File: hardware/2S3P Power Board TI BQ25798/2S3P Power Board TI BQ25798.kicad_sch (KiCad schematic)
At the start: 1 part, among them U1 BQ25798RQMR

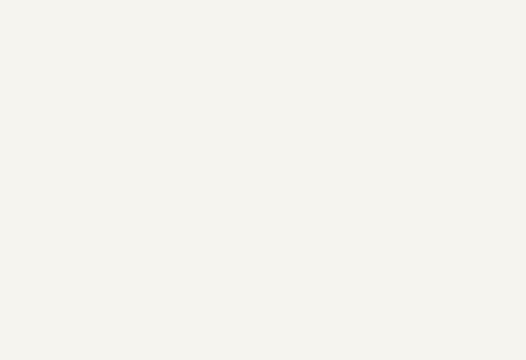
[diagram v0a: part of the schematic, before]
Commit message: Selected USB PD chip
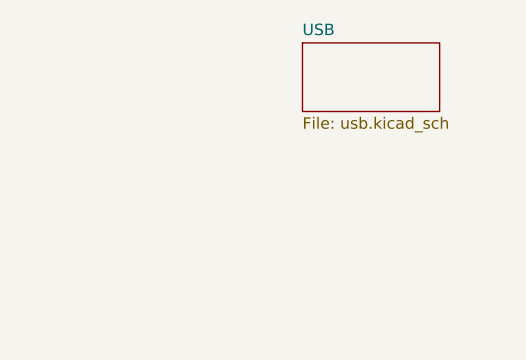
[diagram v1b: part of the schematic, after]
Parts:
- U1: MPN (none) -> C2876593
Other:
- added sheet USB (usb.kicad_sch)
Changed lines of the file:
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@@
       (effects (font (size 1.27 1.27) italic) hide)
+    )
+    (property "MPN" "C2876593" (at 119.38 58.42 0)
+      (effects (font (size 1.27 1.27)) hide)
     )
     (pin "2")
@@
       )
     )
+  )
+  (sheet (at 245.11 16.51) (size 15.24 7.62) (fields_autoplaced)
+    (stroke (width 0.1524) (type solid))
+    (fill (color 0 0 0 0.0000))
+    (property "Sheetname" "USB" (at 245.11 15.7984 0)
+      (effects (font (size 1.27 1.27)) (justify left bottom))
+    )
+    (property "Sheetfile" "usb.kicad_sch" (at 245.11 24.7146 0)
+      (effects (font (size 1.27 1.27)) (justify left top))
+    )
+    (instances
+      (project "2S3P Power Board TI BQ25798"
+        (path "/d7fbba2e-84c5-4e09-9d36-52dae726d12d" (page "2"))
+      )
+    )

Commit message: Checkpointing progress
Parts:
- renumbered U1 to U201
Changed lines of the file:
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@@
   (symbol (lib_id "TI BQ25798:BQ25798RQMR") (at 119.38 58.42 0) (unit 1)
     (in_bom yes) (on_board yes) (dnp no) (fields_autoplaced)
-    (property "Reference" "U1" (at 142.24 48.26 0)
+    (property "Reference" "U201" (at 142.24 48.26 0)
       (effects (font (size 1.524 1.524)))
     )
@@
       (project "2S3P Power Board TI BQ25798"
         (path "/d7fbba2e-84c5-4e09-9d36-52dae726d12d"
-          (reference "U1") (unit 1)
+          (reference "U201") (unit 1)
         )
       )

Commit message: First draft of USB section
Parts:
- U201: Manufacturer (none) -> TEXAS INSTRUMENTS; Manufacturer Part Number (none) -> BQ25798RQMR
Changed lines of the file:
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@@
+      (effects (font (size 1.27 1.27)) hide)
+    )
+    (property "Manufacturer" "TEXAS INSTRUMENTS" (at 119.38 58.42 0)
+      (effects (font (size 1.27 1.27)) hide)
+    )
+    (property "Manufacturer Part Number" "BQ25798RQMR" (at 119.38 58.42 0)
       (effects (font (size 1.27 1.27)) hide)
     )

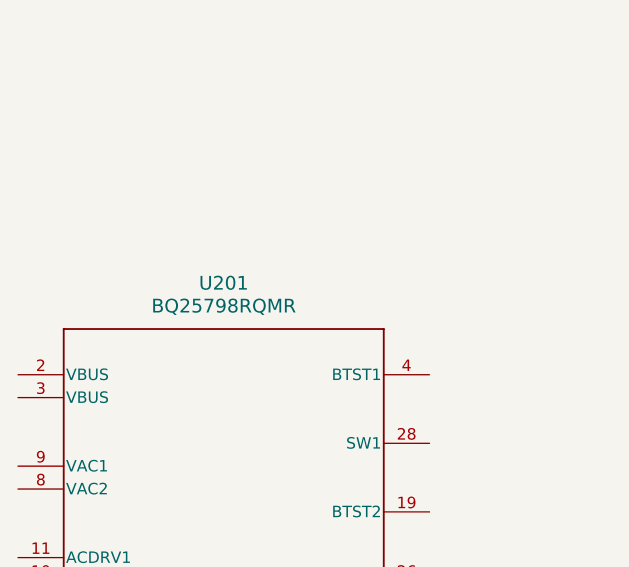
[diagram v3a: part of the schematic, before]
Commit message: Fix part numbering
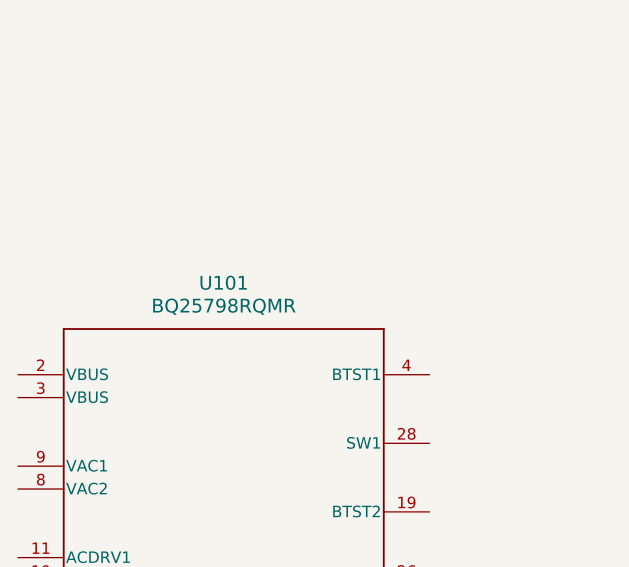
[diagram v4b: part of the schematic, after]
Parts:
- renumbered U201 to U101
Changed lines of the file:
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@@
   (symbol (lib_id "TI BQ25798:BQ25798RQMR") (at 119.38 58.42 0) (unit 1)
     (in_bom yes) (on_board yes) (dnp no) (fields_autoplaced)
-    (property "Reference" "U201" (at 142.24 48.26 0)
+    (property "Reference" "U101" (at 142.24 48.26 0)
       (effects (font (size 1.524 1.524)))
     )
@@
       (project "2S3P Power Board TI BQ25798"
         (path "/d7fbba2e-84c5-4e09-9d36-52dae726d12d"
-          (reference "U201") (unit 1)
+          (reference "U101") (unit 1)
         )
       )

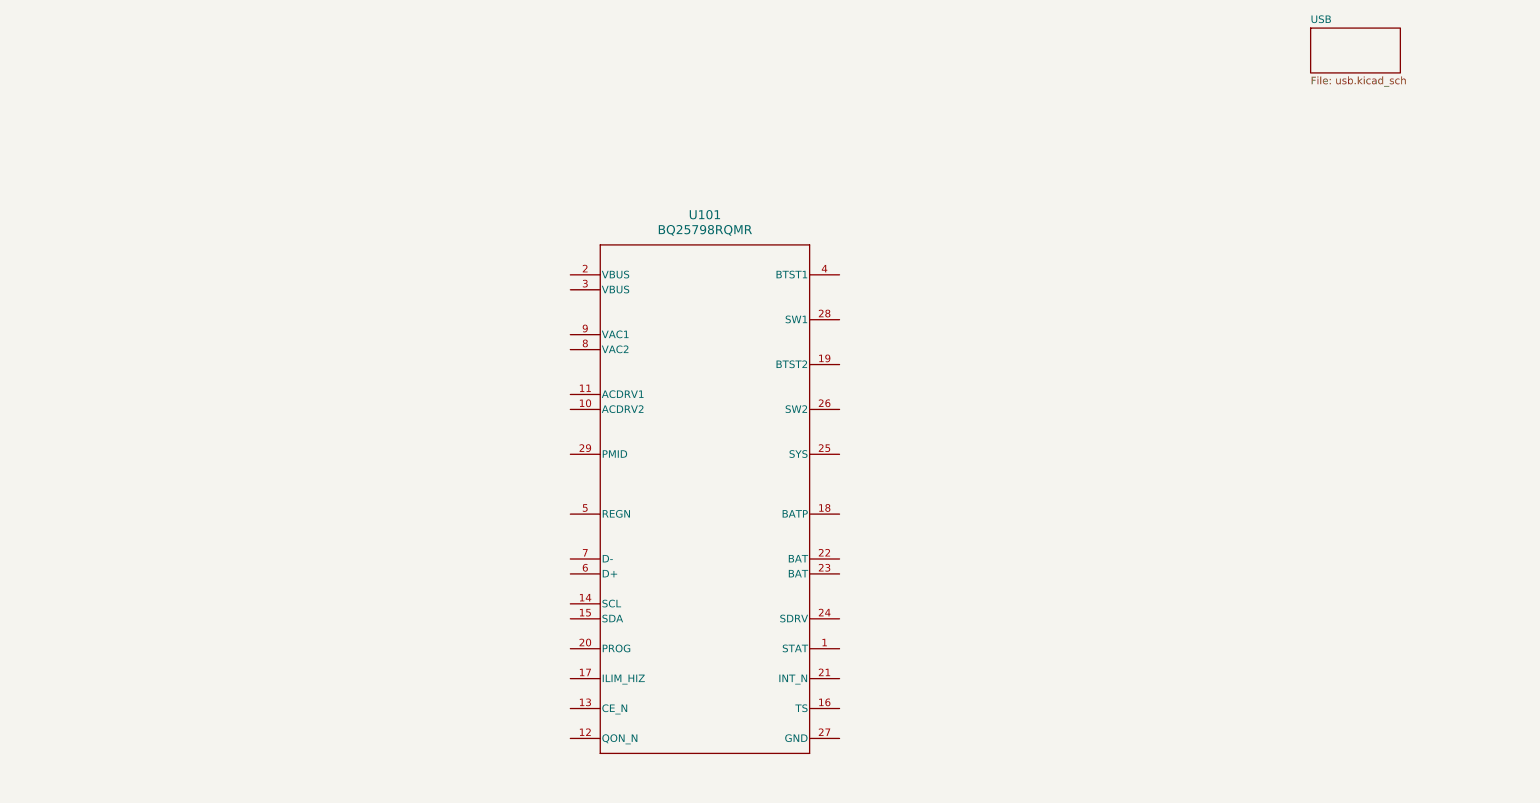
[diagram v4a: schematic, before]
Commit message: Set up input selection into the BQ25798
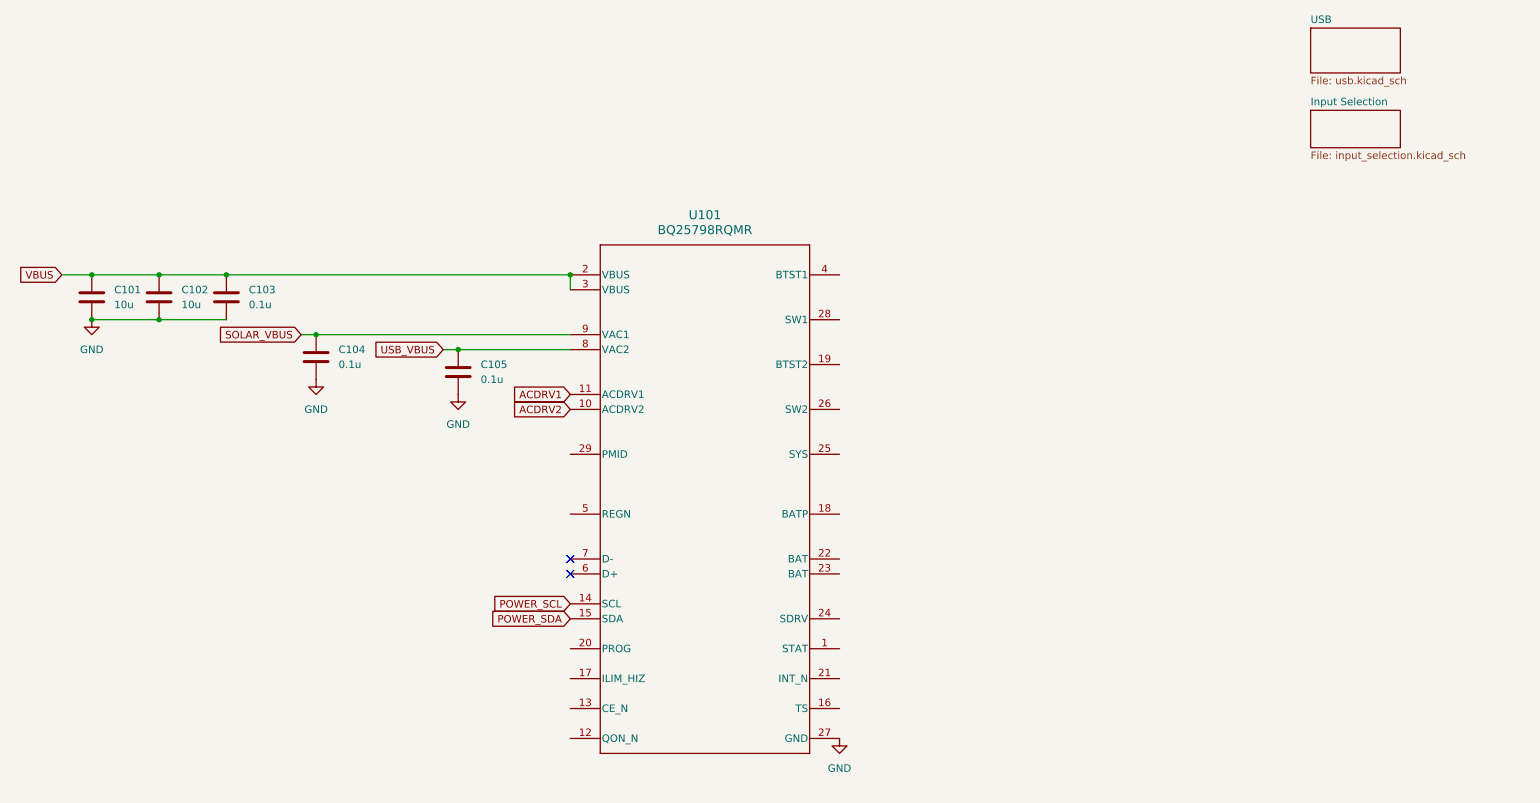
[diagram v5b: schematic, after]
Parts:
- added C101, C102: 10u, Capacitor_SMD:C_0805_2012Metric, symbol Device:C
- added C103, C104, C105: 0.1u, Capacitor_SMD:C_0402_1005Metric, symbol Device:C
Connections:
- net ACDRV2: now reaches U101.10 (ACDRV2)
- net ACDRV1: now reaches U101.11 (ACDRV1)
- net POWER_SCL: now reaches U101.14 (SCL)
- net POWER_SDA: now reaches U101.15 (SDA)
- net VBUS: now reaches U101.2 (VBUS)
- net VBUS: now also U101.3 (VBUS), C101.1, C102.1, C103.1
- net GND: now reaches U101.27 (GND)
- net GND: now also C101.2, C102.2, C103.2, C104.2, C105.2
- net USB_VBUS: now reaches U101.8 (VAC2)
- net USB_VBUS: now also C105.1
- net SOLAR_VBUS: now reaches U101.9 (VAC1)
- net SOLAR_VBUS: now also C104.1
- no-connect marks 0 -> 2
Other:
- added sheet Input Selection (input_selection.kicad_sch)

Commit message: Filled in part numbers
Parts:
- C101, C102: Designed Manufacturer (none) -> TDK; Designed Part Number (none) -> C2012X5R1E106K125AB; MPN (none) -> C386087; Manufacturer TDK -> Taiyo Yuden; Manufacturer Part Number C2012X5R1E106K125AB -> TMK212BJ106KG-TD
- C103, C104, C105: Designed Manufacturer (none) -> TDK; Designed Part Number (none) -> C1005X7R1H104K050BE; MPN (none) -> C5142579; Manufacturer TDK -> CCTC; Manufacturer Part Number C1005X7R1H104K050BE -> TCC0402X5R104K500AT
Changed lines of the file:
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@@
       (effects (font (size 1.27 1.27)) hide)
     )
-    (property "Manufacturer" "TDK" (at 49.53 62.23 0)
-      (effects (font (size 1.27 1.27)) hide)
-    )
-    (property "Manufacturer Part Number" "C2012X5R1E106K125AB " (at 49.53 62.23 0)
+    (property "Manufacturer" "Taiyo Yuden" (at 49.53 62.23 0)
+      (effects (font (size 1.27 1.27)) hide)
+    )
+    (property "Manufacturer Part Number" "TMK212BJ106KG-TD" (at 49.53 62.23 0)
+      (effects (font (size 1.27 1.27)) hide)
+    )
+    (property "Designed Manufacturer" "TDK" (at 49.53 62.23 0)
+      (effects (font (size 1.27 1.27)) hide)
+    )
+    (property "Designed Part Number" "C2012X5R1E106K125AB " (at 49.53 62.23 0)
+      (effects (font (size 1.27 1.27)) hide)
+    )
+    (property "MPN" "C386087" (at 49.53 62.23 0)
       (effects (font (size 1.27 1.27)) hide)
     )
@@
       (effects (font (size 1.27 1.27)) hide)
     )
-    (property "Manufacturer" "TDK" (at 60.96 62.23 0)
-      (effects (font (size 1.27 1.27)) hide)
-    )
-    (property "Manufacturer Part Number" "C1005X7R1H104K050BE" (at 60.96 62.23 0)
+    (property "Manufacturer" "CCTC" (at 60.96 62.23 0)
+      (effects (font (size 1.27 1.27)) hide)
+    )
+    (property "Manufacturer Part Number" "TCC0402X5R104K500AT" (at 60.96 62.23 0)
+      (effects (font (size 1.27 1.27)) hide)
+    )
+    (property "Designed Manufacturer" "TDK" (at 60.96 62.23 0)
+      (effects (font (size 1.27 1.27)) hide)
+    )
+    (property "Designed Part Number" "C1005X7R1H104K050BE" (at 60.96 62.23 0)
+      (effects (font (size 1.27 1.27)) hide)
+    )
+    (property "MPN" "C5142579" (at 60.96 62.23 0)
       (effects (font (size 1.27 1.27)) hide)
     )
@@
       (effects (font (size 1.27 1.27)) hide)
     )
-    (property "Manufacturer" "TDK" (at 38.1 62.23 0)
-      (effects (font (size 1.27 1.27)) hide)
-    )
-    (property "Manufacturer Part Number" "C2012X5R1E106K125AB " (at 38.1 62.23 0)
+    (property "Manufacturer" "Taiyo Yuden" (at 38.1 62.23 0)
+      (effects (font (size 1.27 1.27)) hide)
+    )
+    (property "Manufacturer Part Number" "TMK212BJ106KG-TD" (at 38.1 62.23 0)
+      (effects (font (size 1.27 1.27)) hide)
+    )
+    (property "Designed Manufacturer" "TDK" (at 38.1 62.23 0)
+      (effects (font (size 1.27 1.27)) hide)
+    )
+    (property "Designed Part Number" "C2012X5R1E106K125AB " (at 38.1 62.23 0)
+      (effects (font (size 1.27 1.27)) hide)
+    )
+    (property "MPN" "C386087" (at 38.1 62.23 0)
       (effects (font (size 1.27 1.27)) hide)
     )
@@
       (effects (font (size 1.27 1.27)) hide)
     )
-    (property "Manufacturer" "TDK" (at 100.33 74.93 0)
-      (effects (font (size 1.27 1.27)) hide)
-    )
-    (property "Manufacturer Part Number" "C1005X7R1H104K050BE" (at 100.33 74.93 0)
+    (property "Manufacturer" "CCTC" (at 100.33 74.93 0)
+      (effects (font (size 1.27 1.27)) hide)
+    )
+    (property "Manufacturer Part Number" "TCC0402X5R104K500AT" (at 100.33 74.93 0)
+      (effects (font (size 1.27 1.27)) hide)
+    )
+    (property "Designed Manufacturer" "TDK" (at 100.33 74.93 0)
+      (effects (font (size 1.27 1.27)) hide)
+    )
+    (property "Designed Part Number" "C1005X7R1H104K050BE" (at 100.33 74.93 0)
+      (effects (font (size 1.27 1.27)) hide)
+    )
+    (property "MPN" "C5142579" (at 100.33 74.93 0)
       (effects (font (size 1.27 1.27)) hide)
     )
@@
       (effects (font (size 1.27 1.27)) hide)
     )
-    (property "Manufacturer" "TDK" (at 76.2 72.39 0)
-      (effects (font (size 1.27 1.27)) hide)
-    )
-    (property "Manufacturer Part Number" "C1005X7R1H104K050BE" (at 76.2 72.39 0)
-      (effects (font (size 1.27 1.27)) hide)
-    )
+    (property "Manufacturer" "CCTC" (at 76.2 72.39 0)
+      (effects (font (size 1.27 1.27)) hide)
+    )
+    (property "Manufacturer Part Number" "TCC0402X5R104K500AT" (at 76.2 72.39 0)
+      (effects (font (size 1.27 1.27)) hide)
+    )
+    (property "Designed Manufacturer" "TDK" (at 76.2 72.39 0)
+      (effects (font (size 1.27 1.27)) hide)
+    )
+    (property "Designed Part Number" "C1005X7R1H104K050BE" (at 76.2 72.39 0)
+      (effects (font (size 1.27 1.27)) hide)
+    )
+    (property "MPN" "C5142579" (at 76.2 72.39 0)
+      (effects (font (size 1.27 1.27)) hide)
+    )

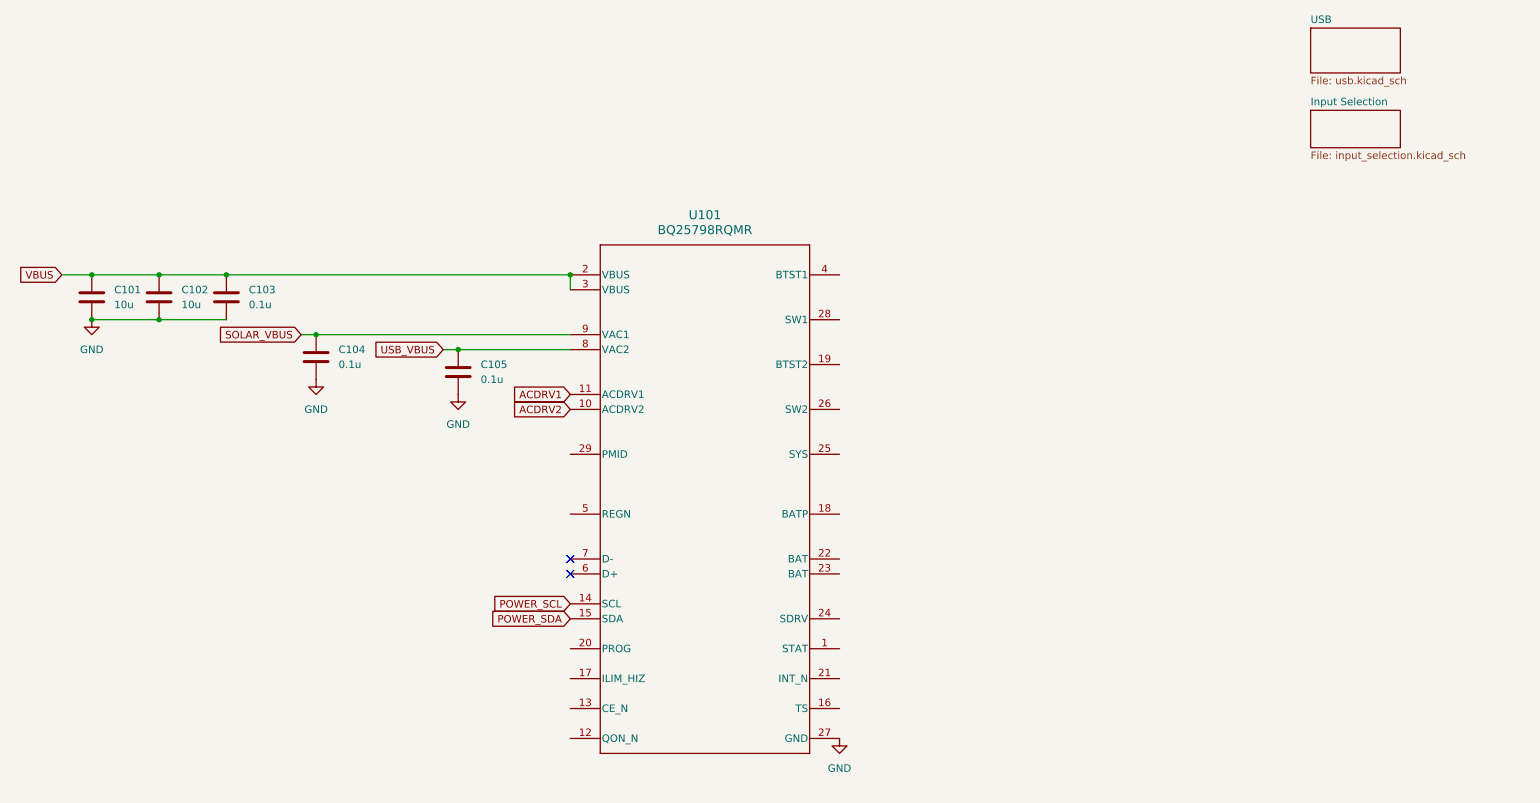
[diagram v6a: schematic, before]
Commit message: Added programming of battery configuration for charging as well as battery temperature monitoring.
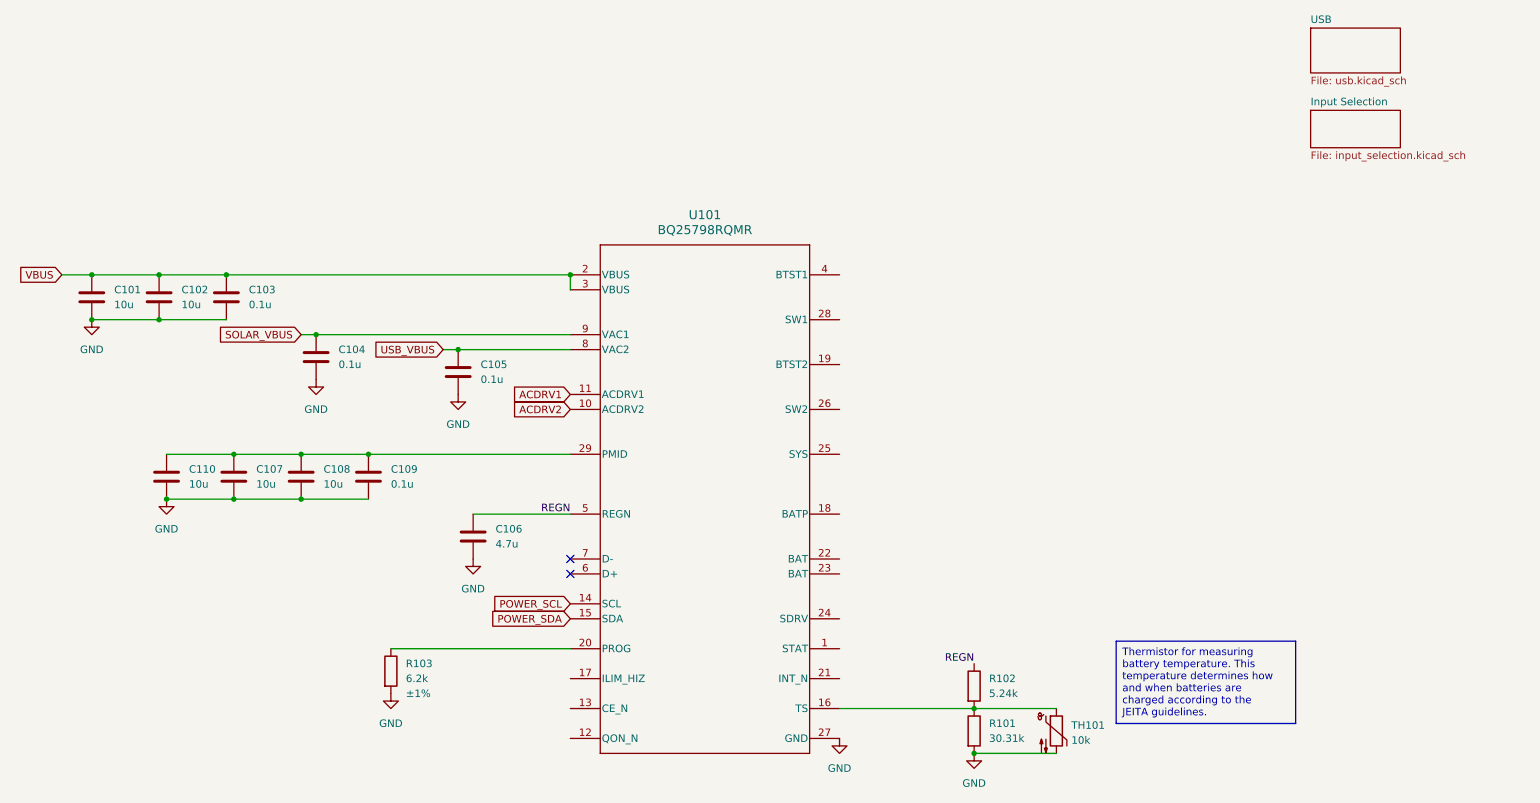
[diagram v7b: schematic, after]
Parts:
- added C106: 4.7u, Capacitor_SMD:C_0201_0603Metric, symbol Device:C
- added C107, C108, C110: 10u, Capacitor_SMD:C_0805_2012Metric, symbol Device:C
- added C109: 0.1u, Capacitor_SMD:C_0402_1005Metric, symbol Device:C
- added R101: 30.31k, Resistor_SMD:R_0603_1608Metric, symbol Device:R
- added R102: 5.24k, Resistor_SMD:R_0402_1005Metric, symbol Device:R
- added R103: 6.2k, Resistor_SMD:R_0603_1608Metric, symbol Device:R
- added TH101: 10k, Resistor_SMD:R_0402_1005Metric, symbol Device:Thermistor_NTC
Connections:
- net GND: now also C106.2, C107.2, C108.2, C109.2, C110.2, R101.2, R103.2, TH101.2
- net at U101.16 (TS): now also R101.1, R102.2, TH101.1
- net at U101.20 (PROG): now also R103.1
- net at U101.29 (PMID): now also C107.1, C108.1, C109.1, C110.1
- net REGN: now reaches U101.5 (REGN)
- net REGN: now also C106.1, R102.1
